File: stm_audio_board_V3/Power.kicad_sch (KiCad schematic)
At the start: 38 parts, among them J5 Barrel_Jack_MountingPin, U1 IS42S16100H-7TL, U2 OP275, U3 MP-K7805-500R3, U4 OP275, U5 MIC2920A-3.3WS-TR, U6 L7809, U9 MIC2920A-3.3WS-TR

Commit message: minor changes
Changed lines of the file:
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@@
   (junction (at 165.1 138.43) (diameter 0) (color 0 0 0 0)
-  )
-  (junction (at 260.35 87.63) (diameter 0) (color 0 0 0 0)
   )
   (junction (at 229.87 104.14) (diameter 0) (color 0 0 0 0)
@@
   )
   (symbol (lib_id "stm_audio:IS42S16100H-7TL") (at 66.04 158.75 0) (unit 2)
-    (in_bom yes) (on_board yes) (dnp no) (fields_autoplaced)
+    (in_bom yes) (on_board yes) (dnp no)
     (property "Reference" "U1" (at 64.4525 148.59 0)
       (effects (font (size 1.27 1.27)))
@@
       (effects (font (size 1.27 1.27)))
     )
-    (property "Footprint" "Library:TSOP-2-50-new" (at 53.975 154.94 0)
-      (effects (font (size 1.27 1.27)))
-    )
+    (property "Footprint" "Library:TSOP-2-50-new" (at 64.135 146.05 0)
+      (effects (font (size 1.27 1.27)))
+    )

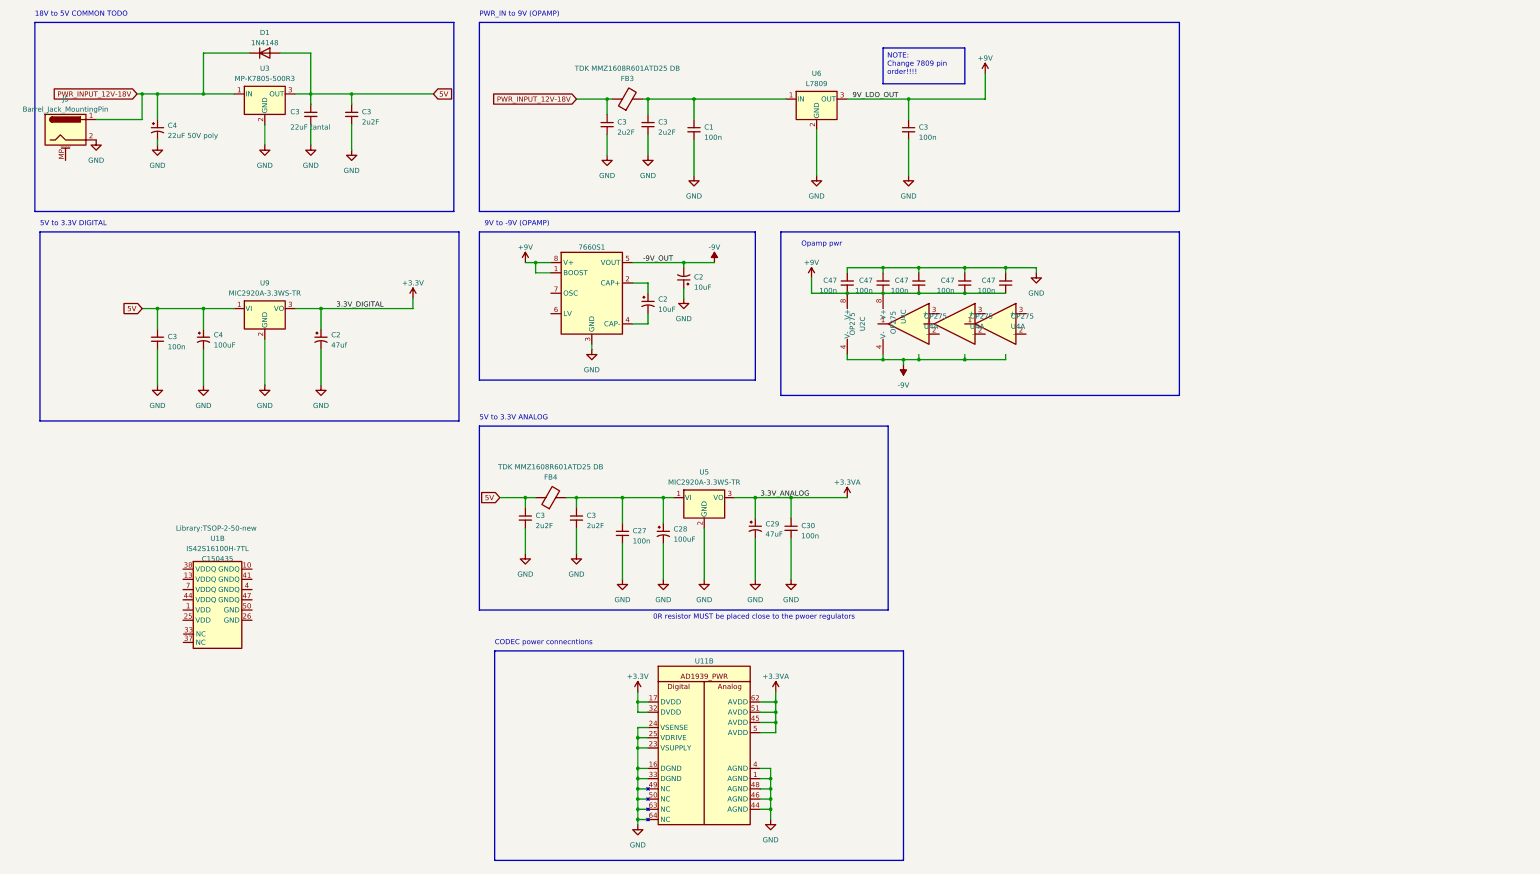
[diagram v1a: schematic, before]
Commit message: +-12 DCDC added
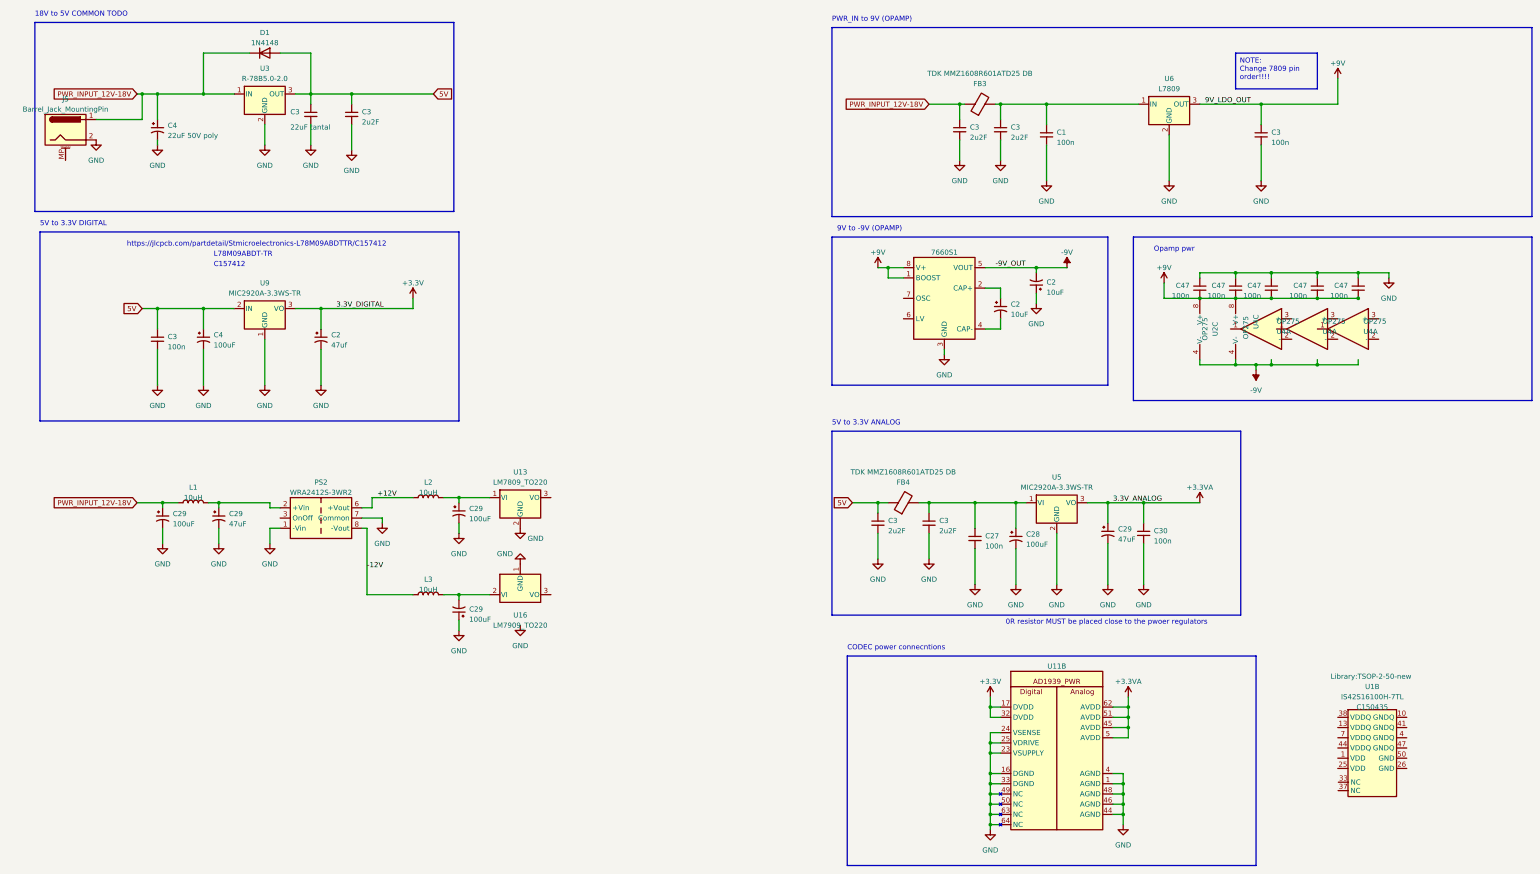
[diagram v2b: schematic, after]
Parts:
- removed U3: MP-K7805-500R3, Package_TO_SOT_THT:TO-220-3_Vertical, symbol Regulator_Linear:L7805
- added C29 (x3): 100uF, Capacitor_THT:CP_Radial_D6.3mm_P2.50mm, symbol Device:C_Polarized_Small_US
- added C29: 47uF, Capacitor_THT:CP_Radial_D6.3mm_P2.50mm, symbol Device:C_Polarized_Small_US
- added L1, L2, L3: 10uH, Inductor_SMD:L_6.3x6.3_H3, symbol Device:L
- added PS2: WRA2412S-3WR2, Converter_DCDC:Converter_DCDC_XP_POWER-ITxxxxxS_THT, symbol Converter_DCDC:ITQ2412S
- added U13: LM7809_TO220, Package_TO_SOT_THT:TO-220-3_Vertical, symbol Regulator_Linear:LM7809_TO220
- added U16: LM7909_TO220, Package_TO_SOT_THT:TO-220-3_Vertical, symbol Regulator_Linear:LM7909_TO220
- added U3: R-78B5.0-2.0, Converter_DCDC:Converter_DCDC_RECOM_R-78B-2.0_THT, symbol Regulator_Switching:R-78B5.0-2.0
- J5: footprint Connector_BarrelJack:BarrelJack_CUI_PJ-063AH_Horizontal -> Connector_BarrelJack:BarrelJack_GCT_DCJ200-10-A_Horizontal
- U9: footprint Package_TO_SOT_SMD:SOT-223-3_TabPin2 -> Package_TO_SOT_SMD:SOT-89-3
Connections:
- net 5V: now also U9.2 (IN), U3.3 (OUT); no longer U9.1 (VI)
- net GND: now also U9.1 (GND), C29.1, C29.2, C29.2, C29.2, PS2.1 (-Vin), PS2.7 (Common), U13.2 (GND), U16.1 (GND), U3.2 (GND); no longer U9.2 (GND)
- net PWR_INPUT_12V-18V: now also C29.1, L1.1, U3.1 (IN)
- new net: C29.1, L1.2, PS2.2 (+Vin)
- new net: C29.2, L3.2, U16.2 (VI)
- new net: C29.1, L2.2, U13.1 (VI)
- new net +12V: L2.1, PS2.6 (+Vout)
- new net -12V: L3.1, PS2.8 (-Vout)
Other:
- note added: "C157412"
- note added: "L78M09ABDT-TR"
- note added: "https://jlcpcb.com/partdetail/Stmicroelectronics-L78M09ABDTTR/C157412"
- moved on the sheet: 7660S1, C1, C2, C27, C28, C29, C3, C30, C47, FB3, FB4, U11B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

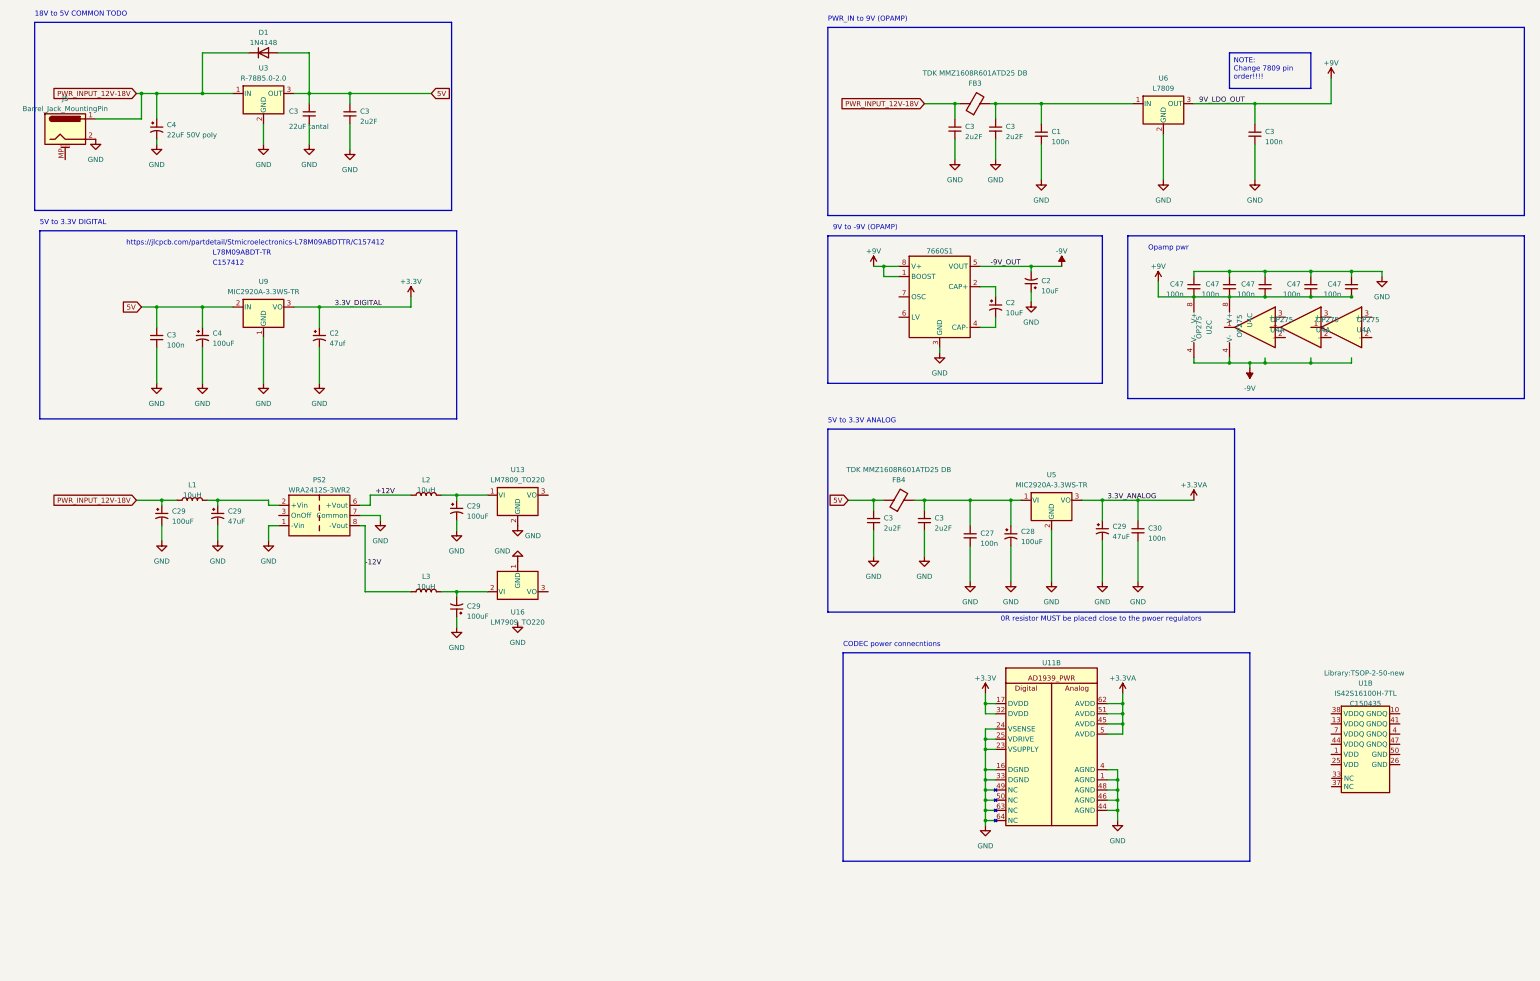
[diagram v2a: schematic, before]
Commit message: isolated power section done
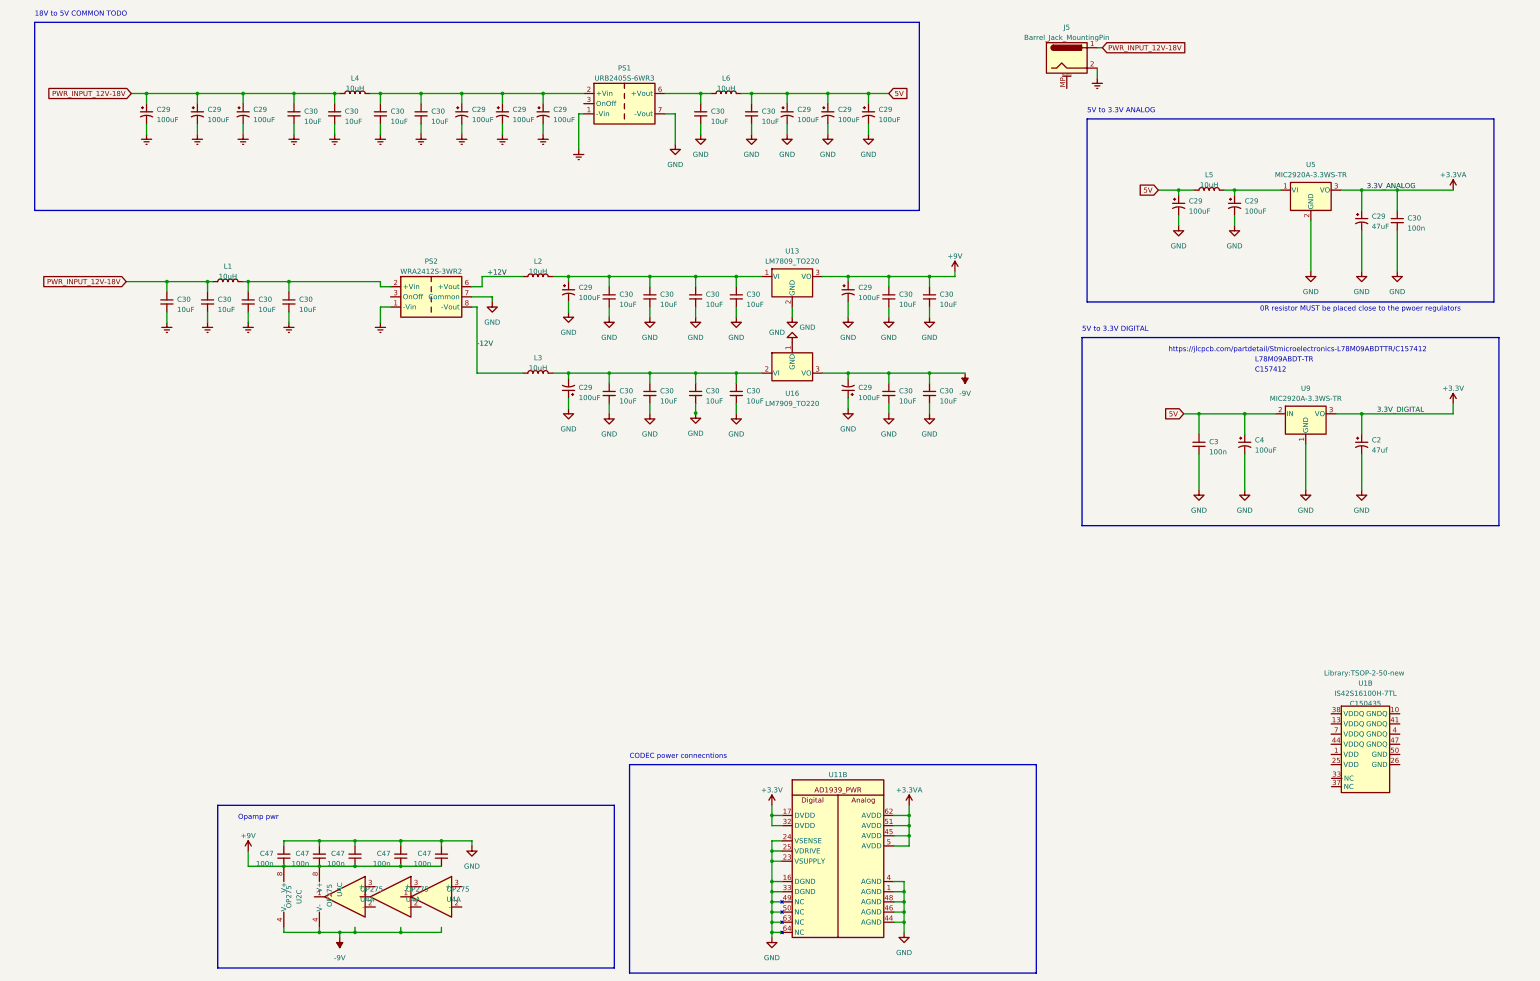
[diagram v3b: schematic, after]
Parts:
- removed 7660S1: ~, Package_SO:SOIC-8_3.9x4.9mm_P1.27mm, symbol stm_audio:7660S
- removed C1, C27, C3: 100n, Capacitor_SMD:C_0603_1608Metric, symbol Device:C_Small
- removed C2 (x2): 10uF, Capacitor_THT:CP_Radial_D5.0mm_P2.00mm, symbol Device:C_Polarized_Small_US
- removed C28, C29: 100uF, Capacitor_THT:CP_Radial_D6.3mm_P2.50mm, symbol Device:C_Polarized_Small_US
- removed C29: 47uF, Capacitor_THT:CP_Radial_D6.3mm_P2.50mm, symbol Device:C_Polarized_Small_US
- removed C3 (x5): 2u2F, Capacitor_SMD:C_0805_2012Metric_Pad1.18x1.45mm_HandSolder, symbol Device:C_Small
- removed C3: 22uF tantal, Capacitor_Tantalum_SMD:CP_EIA-7343-31_Kemet-D_Pad2.25x2.55mm_HandSolder, symbol Device:C_Small
- removed C4: 22uF 50V poly, Capacitor_THT:CP_Radial_D5.0mm_P2.00mm, symbol Device:C_Polarized_Small_US
- removed D1: 1N4148, Diode_SMD:D_1206_3216Metric_Pad1.42x1.75mm_HandSolder, symbol Diode:1N4148
- removed FB3, FB4: TDK MMZ1608R601ATD25 DB, Resistor_SMD:R_0603_1608Metric_Pad0.98x0.95mm_HandSolder, symbol Device:FerriteBead
- removed U3: R-78B5.0-2.0, Converter_DCDC:Converter_DCDC_RECOM_R-78B-2.0_THT, symbol Regulator_Switching:R-78B5.0-2.0
- removed U6: L7809, Package_TO_SOT_THT:TO-92_Inline, symbol Regulator_Linear:L7809
- added C29 (x13): 100uF, Capacitor_THT:CP_Radial_D6.3mm_P2.50mm, symbol Device:C_Polarized_Small_US
- added C30 (x22): 10uF, Capacitor_SMD:C_1206_3216Metric, symbol Device:C_Small
- added L4, L5, L6: 10uH, Inductor_SMD:L_6.3x6.3_H3, symbol Device:L
- added PS1: URB2405S-6WR3, Converter_DCDC:Converter_DCDC_XP_POWER-ITxxxxxS_THT, symbol Converter_DCDC:ITQ2415SA
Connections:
- net +9V: now also U13.3 (VO), C29.1, C30.1, C30.1
- net -9V: now also U16.3 (VO), C29.2, C30.1, C30.1
- net 5V: now also C29.1, C29.1, C29.1, C29.1, C30.1, L5.1, L6.2
- net GND: now also C29.1, C29.2, C29.2, C29.2, C29.2, C29.2, C29.2, C30.2, C30.2, C30.2, C30.2, C30.2, C30.2, C30.2, C30.2, C30.2, C30.2, C30.2, C30.2, C30.2, C30.2, PS1.7 (-Vout); no longer J5.2, PS2.1 (-Vin)
- net PWR_INPUT_12V-18V: now also C29.1, C29.1, C29.1, C30.1, C30.1, C30.1, C30.1, L4.1
- net at L1.2, PS2.2 (+Vin): now also C30.1, C30.1
- net at U5.1 (VI): now also C29.1, L5.2
- net at C29.2, L3.2, U16.2 (VI): now also C30.1, C30.1, C30.1, C30.1
- net at C29.1, L2.2, U13.1 (VI): now also C30.1, C30.1, C30.1, C30.1
- new net: C29.1, C29.1, C29.1, C30.1, C30.1, L4.2, PS1.2 (+Vin)
- new net: C30.1, L6.1, PS1.6 (+Vout)
- new net Earth: C29.2, C29.2, C29.2, C29.2, C29.2, C29.2, C30.2, C30.2, C30.2, C30.2, C30.2, C30.2, C30.2, C30.2, J5.2, PS1.1 (-Vin), PS2.1 (-Vin)
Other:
- note removed: "9V to -9V (OPAMP)"
- note removed: "PWR_IN to 9V (OPAMP)"
- moved on the sheet: C2, C29, C3, C30, C4, C47, J5, L1, L2, L3, PS2, U11B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

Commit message: safety commit
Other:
- moved on the sheet: C29, C30, L2, L3, PS2, U13, U16
